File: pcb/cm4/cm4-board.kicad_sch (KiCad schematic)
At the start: 12 parts, among them J201 DF40C-100DS-0.4V_51_, J202 DF40C-100DS-0.4V_51_, U201 SN74LV1T34DBV

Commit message: update cm4 board
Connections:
- net ETH_GREEN renamed ETH_LED_G
- net ETH_YELLOW renamed ETH_LED_Y
- net TRD0+ renamed ETH_TRD0_P
- net TRD0- renamed ETH_TRD0_M
- net TRD1+ renamed ETH_TRD1_P
- net TRD1- renamed ETH_TRD1_M
- net TRD2+ renamed ETH_TRD2_P
- net TRD2- renamed ETH_TRD2_M
- net TRD3+ renamed ETH_TRD3_P
- net TRD3- renamed ETH_TRD3_M
- net USB+ renamed USB_DP
- net USB- renamed USB_DM
- net USB_OTG_ID renamed USB_ID
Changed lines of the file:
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@@
 		)
 	)
-	(hierarchical_label "TRD2+"
+	(hierarchical_label "ETH_TRD2_P"
 		(shape input)
 		(at 46.99 44.45 180)
@@
 		)
 	)
-	(hierarchical_label "USB-"
+	(hierarchical_label "USB_DM"
 		(shape input)
 		(at 123.19 34.29 180)
@@
 		)
 	)
-	(hierarchical_label "USB+"
+	(hierarchical_label "USB_DP"
 		(shape input)
 		(at 123.19 36.83 180)
@@
 		)
 	)
-	(hierarchical_label "TRD1-"
+	(hierarchical_label "ETH_TRD1_M"
 		(shape input)
 		(at 85.09 36.83 0)
@@
 		)
 	)
-	(hierarchical_label "USB_OTG_ID"
+	(hierarchical_label "USB_ID"
 		(shape input)
 		(at 224.79 46.99 90)
@@
 		)
 	)
-	(hierarchical_label "TRD2-"
+	(hierarchical_label "ETH_TRD2_M"
 		(shape input)
 		(at 46.99 41.91 180)
@@
 		)
 	)
-	(hierarchical_label "TRD1+"
+	(hierarchical_label "ETH_TRD1_P"
 		(shape input)
 		(at 85.09 34.29 0)
@@
 		)
 	)
-	(hierarchical_label "TRD0-"
+	(hierarchical_label "ETH_TRD0_M"
 		(shape input)
 		(at 85.09 41.91 0)
@@
 		)
 	)
-	(hierarchical_label "TRD0+"
+	(hierarchical_label "ETH_TRD0_P"
 		(shape input)
 		(at 85.09 44.45 0)
@@
 		)
 	)
-	(hierarchical_label "ETH_YELLOW"
+	(hierarchical_label "ETH_LED_Y"
 		(shape input)
 		(at 46.99 49.53 180)
@@
 		)
 	)
-	(hierarchical_label "TRD3+"
+	(hierarchical_label "ETH_TRD3_P"
 		(shape input)
 		(at 46.99 34.29 180)
@@
 		)
 	)
-	(hierarchical_label "TRD3-"
+	(hierarchical_label "ETH_TRD3_M"
 		(shape input)
 		(at 46.99 36.83 180)
@@
 		)
 	)
-	(hierarchical_label "ETH_GREEN"
+	(hierarchical_label "ETH_LED_G"
 		(shape input)
 		(at 46.99 52.07 180)

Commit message: update ALL parts
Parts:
- C201: footprint Capacitor_Tantalum_SMD:CP_EIA-7343-43_Kemet-X_Pad2.25x2.55mm_HandSolder -> Capacitor_Tantalum_SMD:CP_EIA-7343-43_Kemet-X; LCSC C7230 -> C132558
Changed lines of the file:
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@@
+			)
+		)
+		(property "MOUSER" ""
+			(at 256.54 124.46 0)
+			(effects
+				(font
+					(size 1.27 1.27)
+				)
 			)
 		)
@@
 			)
 		)
+		(property "MOUSER" ""
+			(at 224.79 66.04 0)
+			(effects
+				(font
+					(size 1.27 1.27)
+				)
+			)
+		)
 		(pin "1"
 		)
@@
 			)
 		)
+		(property "MOUSER" ""
+			(at 199.39 118.11 0)
+			(effects
+				(font
+					(size 1.27 1.27)
+				)
+			)
+		)
 		(pin "1"
 		)
@@
 				)
 				(hide yes)
+			)
+		)
+		(property "MOUSER" ""
+			(at 177.8 64.77 0)
+			(effects
+				(font
+					(size 1.27 1.27)
+				)
 			)
 		)
@@
 			)
 		)
+		(property "MOUSER" ""
+			(at 66.04 92.71 0)
+			(effects
+				(font
+					(size 1.27 1.27)
+				)
+			)
+		)
 		(pin "15"
 		)
@@
 			)
 		)
-		(property "Footprint" "Capacitor_Tantalum_SMD:CP_EIA-7343-43_Kemet-X_Pad2.25x2.55mm_HandSolder"
+		(property "Footprint" "Capacitor_Tantalum_SMD:CP_EIA-7343-43_Kemet-X"
 			(at 102.5652 46.99 0)
 			(effects
@@
 			)
 		)
-		(property "LCSC" "C7230"
+		(property "LCSC" "C132558"
 			(at 101.6 43.18 0)
 			(effects
@@
 				)
 				(hide yes)
+			)
+		)
+		(property "MOUSER" ""
+			(at 101.6 43.18 0)
+			(effects
+				(font
+					(size 1.27 1.27)
+				)
 			)
 		)
@@
 			)
 		)
+		(property "MOUSER" ""
+			(at 231.14 124.46 0)
+			(effects
+				(font
+					(size 1.27 1.27)
+				)
+			)
+		)
 		(pin "4"
 		)
@@
 			)
 		)
+		(property "MOUSER" ""
+			(at 190.5 64.77 0)
+			(effects
+				(font
+					(size 1.27 1.27)
+				)
+			)
+		)
 		(pin "1"
 		)
@@
 			)
 		)
+		(property "MOUSER" ""
+			(at 199.39 128.27 0)
+			(effects
+				(font
+					(size 1.27 1.27)
+				)
+			)
+		)
 		(pin "1"
 		)
@@
 			)
 		)
+		(property "MOUSER" ""
+			(at 138.43 92.71 0)
+			(effects
+				(font
+					(size 1.27 1.27)
+				)
+			)
+		)
 		(pin "2"
 		)
@@
 			)
 		)
+		(property "MOUSER" ""
+			(at 224.79 53.34 0)
+			(effects
+				(font
+					(size 1.27 1.27)
+				)
+			)
+		)
 		(pin "1"
 		)
@@
 			)
 		)
+		(property "MOUSER" ""
+			(at 256.54 114.3 0)
+			(effects
+				(font
+					(size 1.27 1.27)
+				)
+			)
+		)

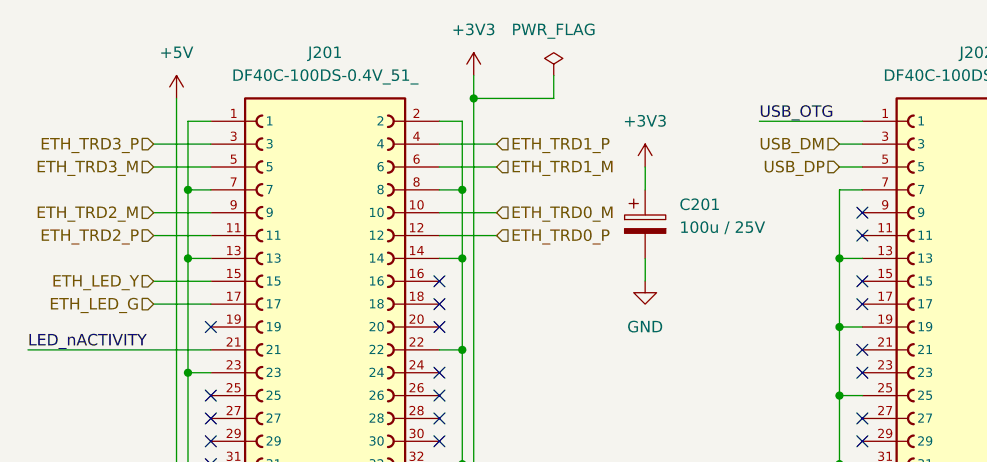
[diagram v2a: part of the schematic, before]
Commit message: rename differential nets correctly and fix cm4 footprint
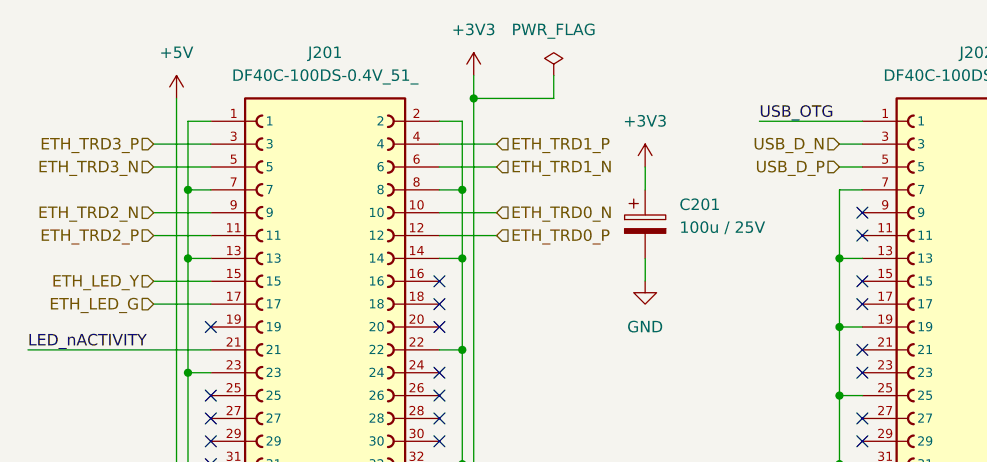
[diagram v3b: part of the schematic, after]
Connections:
- net ETH_TRD0_M renamed ETH_TRD0_N
- net ETH_TRD1_M renamed ETH_TRD1_N
- net ETH_TRD2_M renamed ETH_TRD2_N
- net ETH_TRD3_M renamed ETH_TRD3_N
- net USB_DM renamed USB_D_N
- net USB_DP renamed USB_D_P
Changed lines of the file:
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@@
 		)
 	)
-	(hierarchical_label "USB_DM"
+	(hierarchical_label "USB_D_N"
 		(shape input)
 		(at 123.19 34.29 180)
@@
 		)
 	)
-	(hierarchical_label "USB_DP"
+	(hierarchical_label "USB_D_P"
 		(shape input)
 		(at 123.19 36.83 180)
@@
 		)
 	)
-	(hierarchical_label "ETH_TRD1_M"
+	(hierarchical_label "ETH_TRD1_N"
 		(shape input)
 		(at 85.09 36.83 0)
@@
 		)
 	)
-	(hierarchical_label "ETH_TRD2_M"
+	(hierarchical_label "ETH_TRD2_N"
 		(shape input)
 		(at 46.99 41.91 180)
@@
 		)
 	)
-	(hierarchical_label "ETH_TRD0_M"
+	(hierarchical_label "ETH_TRD0_N"
 		(shape input)
 		(at 85.09 41.91 0)
@@
 		)
 	)
-	(hierarchical_label "ETH_TRD3_M"
+	(hierarchical_label "ETH_TRD3_N"
 		(shape input)
 		(at 46.99 36.83 180)

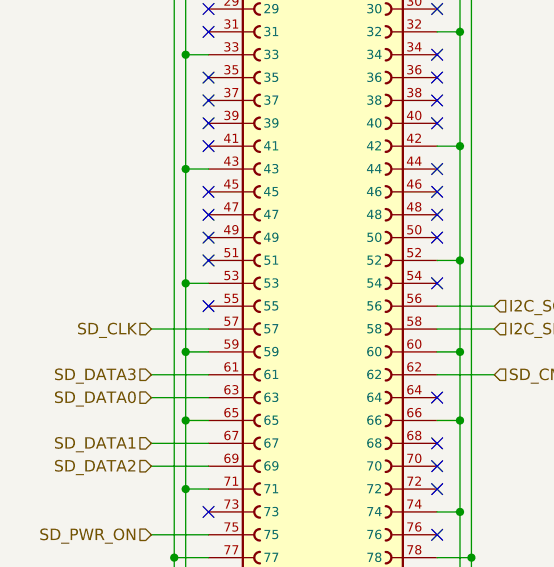
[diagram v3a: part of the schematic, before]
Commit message: cm4: add debug uart
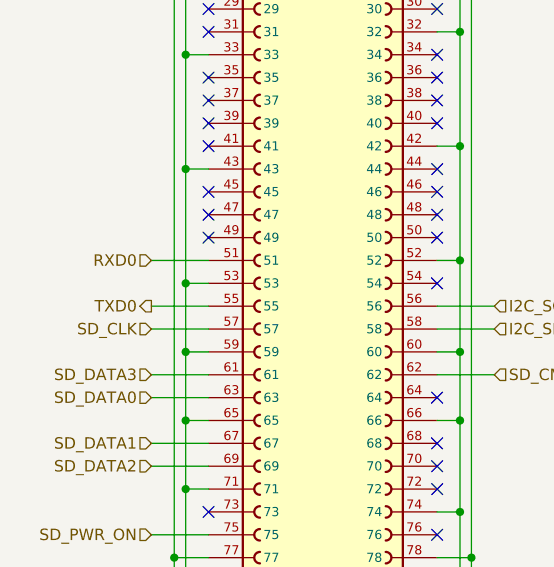
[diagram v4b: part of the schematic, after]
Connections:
- net RXD0: now reaches J201.51
- net TXD0: now reaches J201.55
- no-connect marks 114 -> 112
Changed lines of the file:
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@@
-	)
-	(no_connect
-		(at 53.34 95.25)
 	)
 	(no_connect
@@
 	)
 	(no_connect
-		(at 53.34 100.33)
-	)
-	(no_connect
 		(at 53.34 67.31)
 	)
@@
 	(wire
 		(pts
+			(xy 46.99 100.33) (xy 53.34 100.33)
+		)
+		(stroke
+			(width 0)
+			(type default)
+		)
+	)
+	(wire
+		(pts
 			(xy 78.74 138.43) (xy 82.55 138.43)
 		)
@@
 		(pts
 			(xy 256.54 118.11) (xy 256.54 120.65)
+		)
+		(stroke
+			(width 0)
+			(type default)
+		)
+	)
+	(wire
+		(pts
+			(xy 46.99 95.25) (xy 53.34 95.25)
 		)
 		(stroke
@@
 		)
 	)
+	(hierarchical_label "RXD0"
+		(shape input)
+		(at 46.99 95.25 180)
+		(effects
+			(font
+				(size 1.27 1.27)
+			)
+			(justify right)
+		)
+	)
 	(hierarchical_label "ETH_LED_G"
 		(shape input)
@@
 		(effects
 			(font
+				(size 1.27 1.27)
+			)
+			(justify right)
+		)
+	)
+	(hierarchical_label "TXD0"
+		(shape output)
+		(at 46.99 100.33 180)
+		(effects
+			(font
